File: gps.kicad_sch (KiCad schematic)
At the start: 16 parts, among them J5 SMA, Q1 AO3400A, Q2 AO3401A, U1 MAX-M10S, U15 74LVC1G125

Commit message: Sorting out the part placement....
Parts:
- added C15: 0F22, Capacitor_THT:DX_5R5HxxxxU_D11.5mm_P10.00mm, symbol Device:C_Polarized
- added D15: 1N4148WS, Diode_SMD:D_SOD-323, symbol Diode:1N4148WS
- added R14: 1k, Resistor_SMD:R_0402_1005Metric, symbol Device:R
- TP11, TP12, TP13, TP14: footprint (none) -> Parts:TestPoint
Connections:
- net +3V3: now also D15.2 (A)
- net GND: now also C15.2
- net GPSin: now reaches J5.1 (In), L1.1, U1.11 (RF_IN)
- net V_BCKP: now reaches U1.6 (V_BCKP)
- net V_BCKP: now also D15.1 (K), R14.2
- new net: C15.1, R14.1

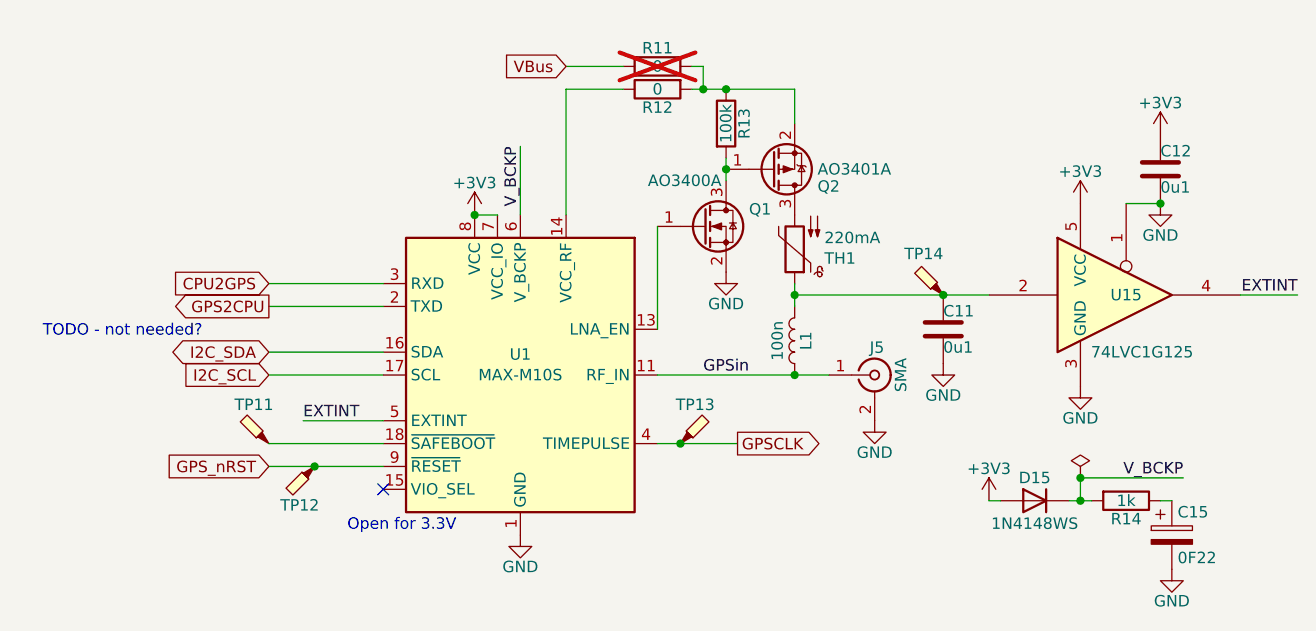
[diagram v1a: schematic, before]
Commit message: First round of component distribution
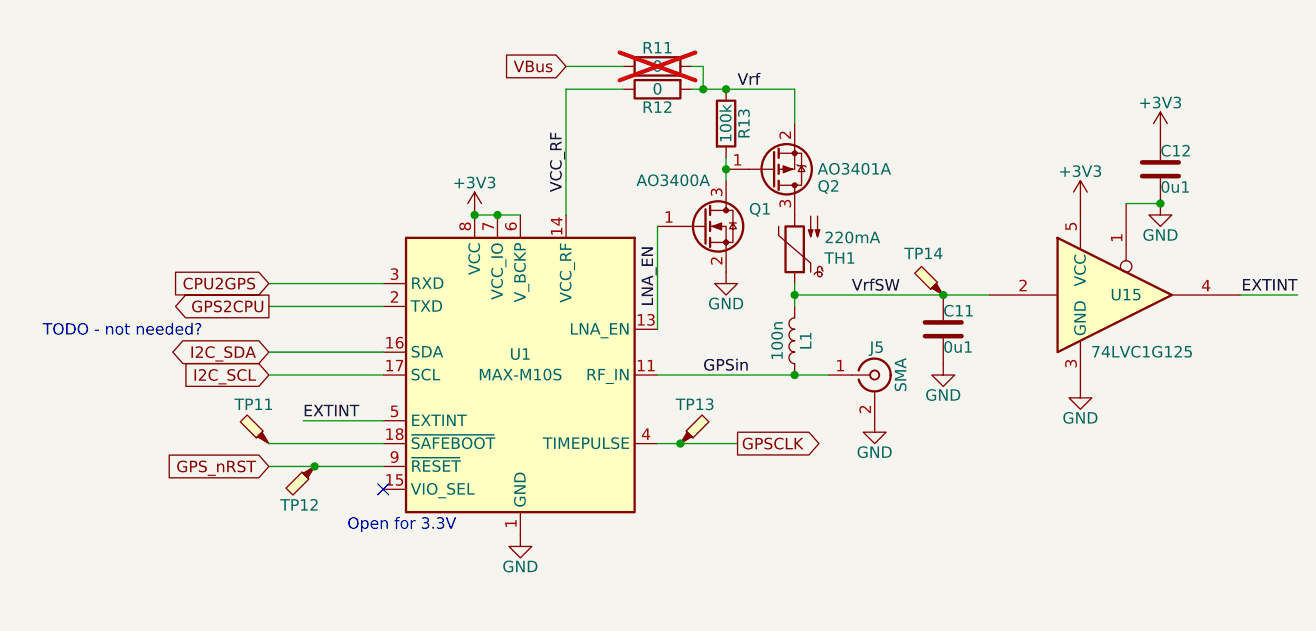
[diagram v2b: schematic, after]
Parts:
- removed C15: 0F22, Capacitor_THT:DX_5R5HxxxxU_D11.5mm_P10.00mm, symbol Device:C_Polarized
- removed D15: 1N4148WS, Diode_SMD:D_SOD-323, symbol Diode:1N4148WS
- removed R14: 1k, Resistor_SMD:R_0402_1005Metric, symbol Device:R
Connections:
- net V_BCKP is gone; now on net +3V3: U1.6 (V_BCKP)
- net VrfSW: now reaches C11.1, L1.2, TH1.1, TP14.1, U15.2
- net LNA_EN: now reaches Q1.1 (G), U1.13 (LNA_EN)
- net Vrf: now reaches Q2.2 (S), R11.2, R12.2, R13.1
- net VCC_RF: now reaches R12.1, U1.14 (VCC_RF)

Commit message: Placement looks sane.
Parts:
- U15: value 74LVC1G125 -> 74LVC1G07; footprint Package_TO_SOT_SMD:SOT-353_SC-70-5 -> Package_TO_SOT_SMD:SOT-23-5; symbol 74xGxx:74LVC1G125 -> 74xGxx:74LVC1G07; now in the parts list
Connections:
- net +3V3: no longer U1.6 (V_BCKP)
- net GND: no longer U15.1
- net I2C_SCL: now also U1.16 (SDA); no longer U1.17 (SCL)
- net I2C_SDA: now also U1.17 (SCL); no longer U1.16 (SDA)
- no-connect marks 1 -> 3
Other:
- note added: "TODO - restore supercap?"
- note removed: "TODO - not needed?"
- moved on the sheet: TP12

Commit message: Routing well underway
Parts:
- removed TP11, TP13: TestPoint_Probe, Parts:TestPoint, symbol Connector:TestPoint_Probe
- L1: footprint Inductor_SMD:L_0402_1005Metric -> Parts:HHS_0402
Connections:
- net I2C_SCL: no longer names the net of U1.16 (SDA)
- net I2C_SDA: no longer names the net of U1.17 (SCL)
- no-connect marks 3 -> 6

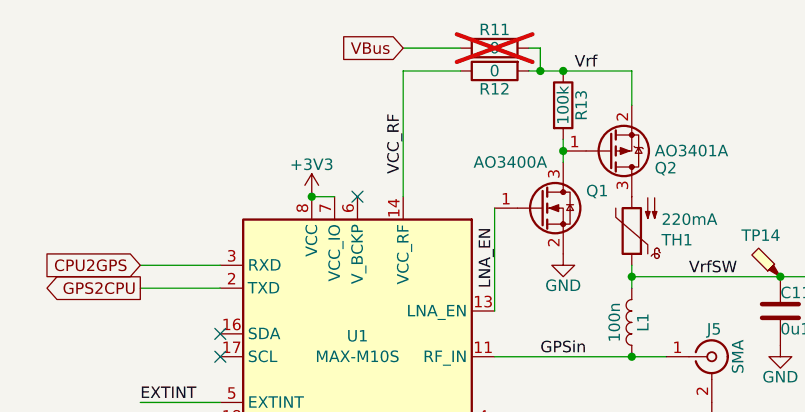
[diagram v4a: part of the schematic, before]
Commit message: Supercap is back
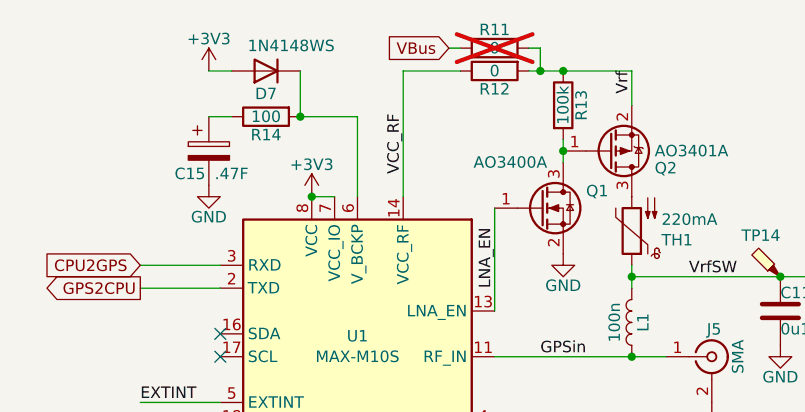
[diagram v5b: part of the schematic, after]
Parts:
- added C15: .47F, Parts:CP_Radial_D13.5mm_P5.00mm, symbol Device:C_Polarized
- added D7: 1N4148WS, Diode_SMD:D_SOD-323, symbol Diode:1N4148WS
- added R14: 100, Resistor_SMD:R_0402_1005Metric, symbol Device:R
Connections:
- net +3V3: now also D7.2 (A)
- net GND: now also C15.2
- net at U1.6 (V_BCKP): now also D7.1 (K), R14.2
- new net: C15.1, R14.1
- no-connect marks 6 -> 5

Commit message: Down to the dregs and clean-ups.
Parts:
- added L11: 220, Inductor_SMD:L_0603_1608Metric, symbol Parts:L_Ferrite_Power
- C11, C12: JLCPCB (none) -> C307331
- D7: JLCPCB (none) -> C2128
- Q1: JLCPCB (none) -> C20917
- Q2: JLCPCB (none) -> C15127
- R12: JLCPCB (none) -> C21189
- R13: JLCPCB (none) -> C25741
- R14: JLCPCB (none) -> C25076
- TH1, U15: now left out of the parts list
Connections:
- net VBus: now also L11.1; no longer R11.1
- net VBCKP: now reaches D7.1 (K), R14.2, U1.6 (V_BCKP)
- new net: L11.2, R11.1
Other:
- note removed: "TODO - restore supercap?"
- moved on the sheet: R11
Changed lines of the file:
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@@
-		)
-	)
-	(text "TODO - restore supercap?"
-		(exclude_from_sim no)
-		(at 127.762 111.506 0)
-		(effects
-			(font
-				(size 1.27 1.27)
-			)
 		)
 	)
@@
 	)
 	(junction
-		(at 120.65 67.31)
-		(diameter 0)
-		(color 0 0 0 0)
-	)
-	(junction
 		(at 93.98 72.39)
 		(diameter 0)
@@
 	(wire
 		(pts
-			(xy 111.76 64.77) (xy 110.49 64.77)
-		)
-		(stroke
-			(width 0)
-			(type default)
-		)
-	)
-	(wire
-		(pts
 			(xy 123.19 67.31) (xy 130.81 67.31)
 		)
@@
 	(wire
 		(pts
-			(xy 120.65 64.77) (xy 119.38 64.77)
-		)
-		(stroke
-			(width 0)
-			(type default)
-		)
-	)
-	(wire
-		(pts
 			(xy 130.81 67.31) (xy 130.81 71.12)
 		)
@@
 	(wire
 		(pts
-			(xy 120.65 64.77) (xy 120.65 67.31)
+			(xy 123.19 63.5) (xy 123.19 67.31)
 		)
 		(stroke
@@
 	(wire
 		(pts
-			(xy 120.65 67.31) (xy 123.19 67.31)
-		)
-		(stroke
-			(width 0)
-			(type default)
-		)
-	)
-	(wire
-		(pts
 			(xy 83.82 72.39) (xy 86.36 72.39)
 		)
@@
 	(wire
 		(pts
-			(xy 119.38 67.31) (xy 120.65 67.31)
+			(xy 119.38 67.31) (xy 123.19 67.31)
 		)
 		(stroke
@@
 	(label "EXTINT"
 		(at 76.2 104.14 0)
+		(effects
+			(font
+				(size 1.27 1.27)
+			)
+			(justify left bottom)
+		)
+	)
+	(label "VBCKP"
+		(at 95.25 72.39 0)
 		(effects
 			(font
@@
 	(global_label "VBus"
 		(shape input)
-		(at 110.49 64.77 180)
-		(fields_autoplaced yes)
+		(at 107.95 63.5 180)
 		(effects
 			(font
@@
 		)
 		(property "Intersheetrefs" "${INTERSHEET_REFS}"
-			(at 102.9691 64.77 0)
+			(at 102.2071 63.5 0)
 			(effects
 				(font
@@
 		(unit 1)
 		(exclude_from_sim no)
-		(in_bom yes)
+		(in_bom no)
 		(on_board yes)
 		(dnp no)
@@
 			)
 		)
+		(property "JLCPCB" "C20917"
+			(at 120.65 82.55 0)
+			(effects
+				(font
+					(size 1.27 1.27)
+				)
+				(hide yes)
+			)
+		)
 		(pin "2"
 		)
@@
 	(symbol
 		(lib_id "Device:R")
-		(at 115.57 64.77 90)
+		(at 119.38 63.5 90)
 		(unit 1)
 		(exclude_from_sim no)
@@
 		(dnp yes)
 		(property "Reference" "R11"
-			(at 115.57 62.738 90)
+			(at 119.38 61.468 90)
 			(effects
 				(font
@@
 		)
 		(property "Value" "0"
-			(at 115.57 64.77 90)
+			(at 119.38 63.5 90)
 			(effects
 				(font
@@
 		)
 		(property "Footprint" "Resistor_SMD:R_0603_1608Metric"
-			(at 115.57 66.548 90)
+			(at 119.38 65.278 90)
 			(effects
 				(font
@@
 		)
 		(property "Datasheet" ""
-			(at 115.57 64.77 0)
+			(at 119.38 63.5 0)
 			(effects
 				(font
@@
 		)
 		(property "Description" "Resistor"
-			(at 115.57 64.77 0)
+			(at 119.38 63.5 0)
 			(effects
 				(font
@@
 		)
 		(property "JLCPCB" ""
-			(at 115.57 64.77 0)
+			(at 119.38 63.5 0)
 			(effects
 				(font
@@
 			)
 		)
-		(property "JLCPCB" ""
+		(property "JLCPCB" "C25076"
 			(at 90.17 72.39 0)
 			(effects
@@
 		)
 		(property "Value" "1N4148WS"
-			(at 92.964 64.516 0)
+			(at 91.44 65.024 0)
 			(effects
 				(font
@@
 			)
 		)
+		(property "JLCPCB" "C2128"
+			(at 90.17 67.31 0)
+			(effects
+				(font
+					(size 1.27 1.27)
+				)
+				(hide yes)
+			)
+		)
 		(pin "2"
 		)
@@
 		(unit 1)
 		(exclude_from_sim no)
-		(in_bom yes)
+		(in_bom no)
 		(on_board yes)
 		(dnp no)
@@
 				(path "/3160ff17-81c2-4674-af97-e8d9acaf6b65/69331f4b-e5ad-4452-8850-5c5a77857efb"
 					(reference "U15")
+					(unit 1)
+				)
+			)
+		)
+	)
+	(symbol
+		(lib_id "Parts:L_Ferrite_Power")
+		(at 111.76 63.5 90)
+		(unit 1)
+		(exclude_from_sim no)
+		(in_bom yes)
+		(on_board yes)
+		(dnp no)
+		(property "Reference" "L11"
+			(at 111.76 64.77 90)
+			(effects
+				(font
+					(size 1.27 1.27)
+				)
+			)
+		)
+		(property "Value" "220"
+			(at 111.76 60.706 90)
+			(effects
+				(font
+					(size 1.27 1.27)
+				)
+			)
+		)
+		(property "Footprint" "Inductor_SMD:L_0603_1608Metric"
+			(at 111.76 63.5 0)
+			(effects
+				(font
+					(size 1.27 1.27)
+				)
+				(hide yes)
+			)
+		)
+		(property "Datasheet" "~"
+			(at 111.76 63.5 0)
+			(effects
+				(font
+					(size 1.27 1.27)
+				)
+				(hide yes)
+			)
+		)
+		(property "Description" "Inductor with ferrite core"
+			(at 111.76 63.5 0)
+			(effects
+				(font
+					(size 1.27 1.27)
+				)
+				(hide yes)
+			)
+		)
+		(property "JLCPCB" "C14709"
+			(at 111.76 63.5 90)
+			(effects
+				(font
+					(size 1.27 1.27)
+				)
+				(hide yes)
+			)
+		)
+		(pin "1"
+		)
+		(pin "2"
+		)
+		(instances
+			(project "gpsref"
+				(path "/3160ff17-81c2-4674-af97-e8d9acaf6b65/69331f4b-e5ad-4452-8850-5c5a77857efb"
+					(reference "L11")
 					(unit 1)
 				)
@@
 			)
 		)
-		(property "Datasheet" ""
+		(property "Datasheet" "~"
 			(at 115.57 67.31 0)
 			(effects
@@
 			)
 		)
-		(property "JLCPCB" ""
+		(property "JLCPCB" "C21189"
 			(at 115.57 67.31 0)
 			(effects
@@
 			)
 		)
+		(property "JLCPCB" "C307331"
+			(at 171.45 76.2 0)
+			(effects
+				(font
+					(size 1.27 1.27)
+				)
+				(hide yes)
+			)
+		)
 		(pin "1"
 		)
@@
 		)
 		(property "Description" "Unpolarized capacitor"
+			(at 147.32 93.98 0)
+			(effects
+				(font
+					(size 1.27 1.27)
+				)
+				(hide yes)
+			)
+		)
+		(property "JLCPCB" "C307331"
 			(at 147.32 93.98 0)
 			(effects
@@
 			)
 		)
+		(property "JLCPCB" "C15127"
+			(at 128.27 76.2 0)
+			(effects
+				(font
+					(size 1.27 1.27)
+				)
+				(hide yes)
+			)
+		)
 		(pin "1"
 		)
@@
 			(effects
 				(font
+					(size 1.27 1.27)
+				)
+				(hide yes)
+			)
+		)
+		(property "JLCPCB" "C25741"
+			(at 123.19 71.12 90)
+			(effects
+				(font

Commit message: Add a U.Fl connector for fun.
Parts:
- renumbered J5 to J6
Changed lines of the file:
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@@
+	)
+	(junction
+		(at 100.33 74.93)
+		(diameter 0)
+		(color 0 0 0 0)
 	)
 	(junction
@@
 	(wire
 		(pts
+			(xy 100.33 74.93) (xy 100.33 72.39)
+		)
+		(stroke
+			(width 0)
+			(type default)
+		)
+	)
+	(wire
+		(pts
 			(xy 123.19 67.31) (xy 130.81 67.31)
 		)
@@
 	(wire
 		(pts
-			(xy 100.33 81.28) (xy 100.33 72.39)
+			(xy 100.33 81.28) (xy 100.33 74.93)
 		)
 		(stroke
@@
 		(on_board yes)
 		(dnp no)
-		(property "Reference" "J5"
+		(property "Reference" "J6"
 			(at 139.954 96.012 0)
 			(effects
@@
 			(project "gpsref"
 				(path "/3160ff17-81c2-4674-af97-e8d9acaf6b65/69331f4b-e5ad-4452-8850-5c5a77857efb"
-					(reference "J5")
+					(reference "J6")
 					(unit 1)
 				)
@@
 					(unit 1)
 				)
+			)
+		)
+	)
+	(symbol
+		(lib_id "power:PWR_FLAG")
+		(at 100.33 74.93 90)
+		(unit 1)
+		(exclude_from_sim no)
+		(in_bom yes)
+		(on_board yes)
+		(dnp no)
+		(property "Reference" "#FLG071"
+			(at 98.425 74.93 0)
+			(effects
+				(font
+					(size 1.27 1.27)
+				)
+				(hide yes)
+			)
+		)
+		(property "Value" "PWR_FLAG"
+			(at 96.52 74.93 0)
+			(effects
+				(font
+					(size 1.27 1.27)
+				)
+				(hide yes)
+			)
+		)
+		(property "Footprint" ""
+			(at 100.33 74.93 0)
+			(effects
+				(font
+					(size 1.27 1.27)
+				)
+				(hide yes)
+			)
+		)
+		(property "Datasheet" "~"
+			(at 100.33 74.93 0)
+			(effects
+				(font
+					(size 1.27 1.27)
+				)
+				(hide yes)
+			)
+		)
+		(property "Description" "Special symbol for telling ERC where power comes from"
+			(at 100.33 74.93 0)
+			(effects
+				(font
+					(size 1.27 1.27)
+				)
+				(hide yes)
+			)
+		)
+		(pin "1"
+		)
+		(instances
+			(project ""
+				(path "/3160ff17-81c2-4674-af97-e8d9acaf6b65/69331f4b-e5ad-4452-8850-5c5a77857efb"
+					(reference "#FLG071")
+					(unit 1)
+				)

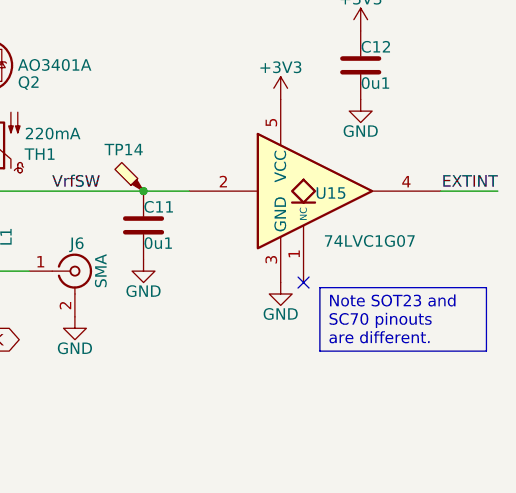
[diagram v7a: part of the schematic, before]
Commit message: DRC clean-up.  Only silk-screen noise left.
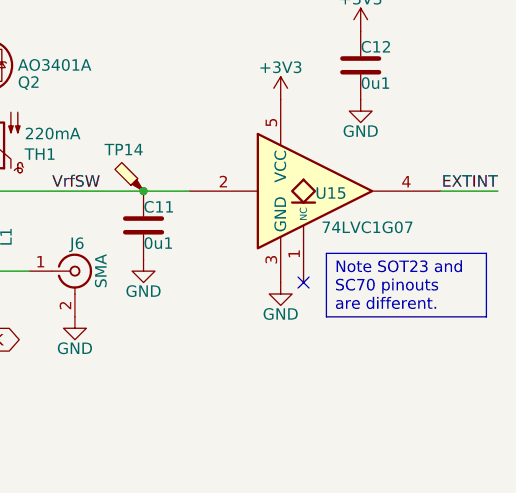
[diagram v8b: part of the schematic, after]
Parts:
- J6: footprint Connector_Coaxial:SMA_Amphenol_132289_EdgeMount -> Parts:SMA_Amphenol_132289_EdgeMount
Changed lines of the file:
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@@
 	(text_box "Note SOT23 and SC70 pinouts are different."
 		(exclude_from_sim no)
-		(at 166.9213 100.8959 0)
-		(size 18.4987 7.0541)
+		(at 167.6399 97.0859 0)
+		(size 17.7801 7.0541)
 		(margins 0.9525 0.9525 0.9525 0.9525)
 		(stroke
@@
 			)
 		)
-		(property "Footprint" "Connector_Coaxial:SMA_Amphenol_132289_EdgeMount"
+		(property "Footprint" "Parts:SMA_Amphenol_132289_EdgeMount"
 			(at 139.7 99.06 0)
 			(effects
@@
 		)
 		(property "Value" "74LVC1G07"
-			(at 172.466 95.758 0)
-			(effects
-				(font
+			(at 172.212 94.234 0)
+			(effects
+				(font
